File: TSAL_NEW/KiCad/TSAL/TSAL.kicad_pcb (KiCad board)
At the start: 2 copper layers, 74.8 x 41.9 mm, 33 parts, among them J1 HV INPUT, J2 HV GND, J3 Pin Storage, J4 Green_LED_Jp, J5 Conn_02x02_Counter_Clockwise, Q1 BSS84, Q2 BSS84, U1 LTV-817S, U2 LR8K4-G, U4 LM555

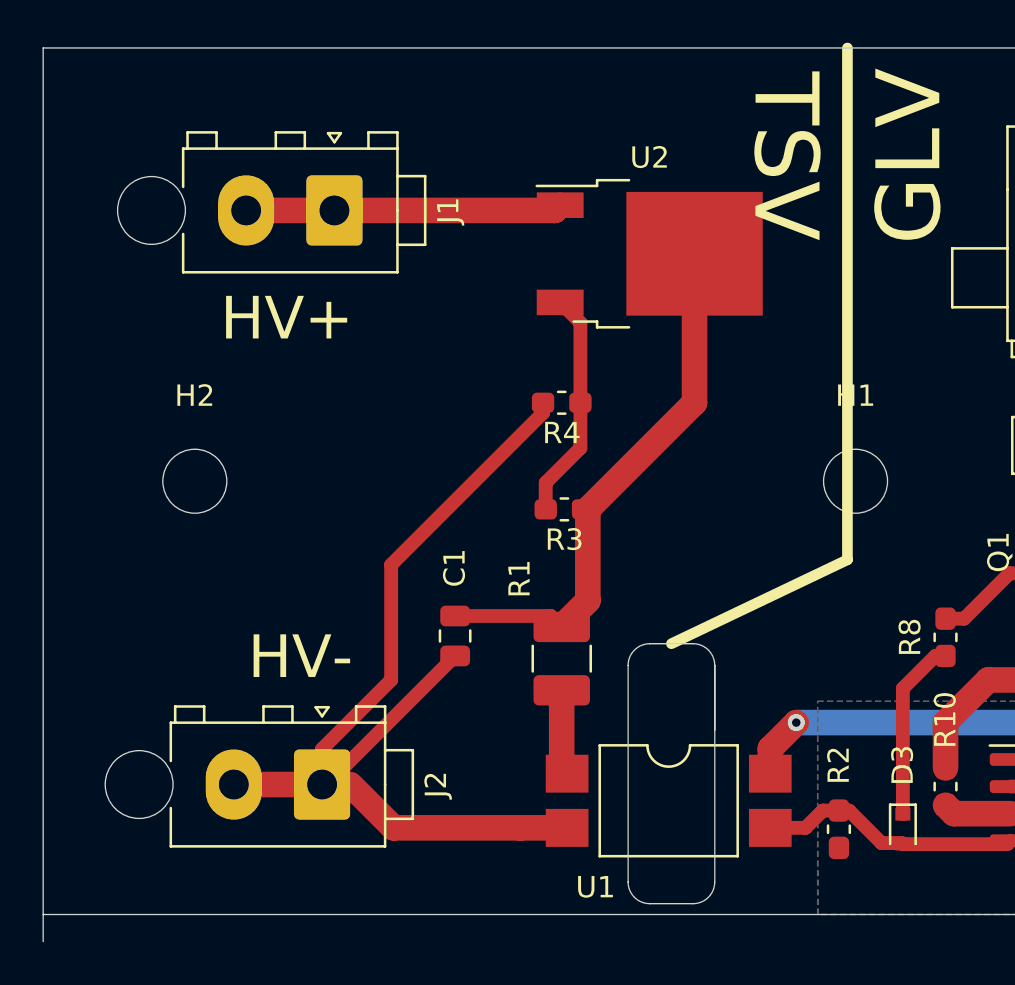
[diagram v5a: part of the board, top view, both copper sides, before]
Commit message: Added logos
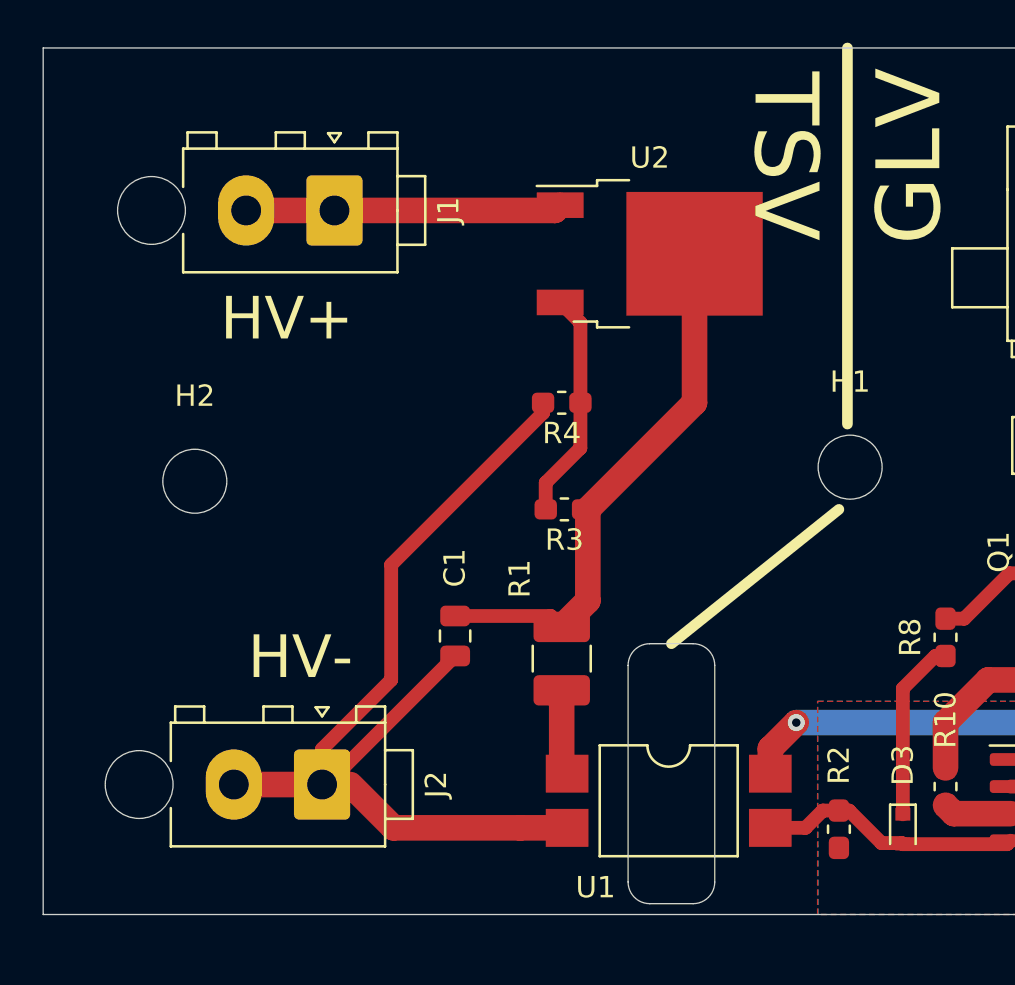
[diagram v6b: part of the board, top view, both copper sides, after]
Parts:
- added G***: LOGO, AERO-footprints:AERO_Logo_15x6mm, B.Cu at (168.0, 120.5)
- moved H1 0.71 mm to (144.5, 106.0)
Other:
- board size 74.8 x 41.9 mm -> 74.8 x 40.6 mm
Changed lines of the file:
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@@
   (general
     (thickness 1.6)
-    (drawings 27)
+    (drawings 26)
     (tracks 116)
     (zones 0)
-    (modules 33)
+    (modules 34)
     (nets 24)
   )
@@
   )
   (setup
-    (last_trace_width 0.65)
+    (last_trace_width 0.25)
     (user_trace_width 0.24)
     (user_trace_width 0.36)
@@
     (add_net GNDA)
   )
+  (module AERO-footprints:AERO_Logo_15x6mm (layer B.Cu)
+    (at 168 120.5 180)
+    (fp_text reference G*** (at 0 0) (layer B.SilkS) hide
+      (effects (font (size 1.524 1.524) (thickness 0.3)) (justify mirror))
+    )
+    (fp_text value LOGO (at 0.75 0) (layer B.SilkS) hide
+      (effects (font (size 1.524 1.524) (thickness 0.3)) (justify mirror))
+    )
+    (fp_poly (pts (xy 6.892292 2.256606) (xy 7.522038 1.627588) (xy 7.522038 -1.522592) (xy 6.209332 -2.833934)
+      (xy 5.038016 -1.661096) (xy 5.038016 -1.378625) (xy 5.912672 -1.378625) (xy 6.024987 -1.494504)
+      (xy 6.137301 -1.610384) (xy 6.374849 -1.374656) (xy 6.612397 -1.138929) (xy 6.612397 1.208337)
+      (xy 6.262534 1.556887) (xy 5.912672 1.905436) (xy 5.912672 -1.378625) (xy 5.038016 -1.378625)
+      (xy 5.038016 1.662595) (xy 5.650281 2.27411) (xy 6.262545 2.885624) (xy 6.892292 2.256606)) (layer B.SilkS) (width 0.01))
+    (fp_poly (pts (xy 4.085094 2.369879) (xy 4.583195 1.870887) (xy 4.583195 0.963505) (xy 3.972357 0.349823)
+      (xy 4.295269 0.025563) (xy 4.618182 -0.298698) (xy 4.618182 -1.659646) (xy 4.801166 -1.844931)
+      (xy 4.984149 -2.030217) (xy 4.180096 -2.83427) (xy 3.395312 -2.046694) (xy 3.567904 -1.85427)
+      (xy 3.740497 -1.661846) (xy 3.742011 -1.206428) (xy 3.743526 -0.751011) (xy 3.358678 -0.367356)
+      (xy 2.973829 0.0163) (xy 2.973829 -1.699463) (xy 3.149146 -1.872144) (xy 3.324464 -2.044825)
+      (xy 2.931053 -2.439355) (xy 2.796179 -2.57326) (xy 2.678343 -2.687693) (xy 2.586396 -2.774262)
+      (xy 2.529184 -2.824577) (xy 2.515023 -2.833884) (xy 2.484378 -2.809858) (xy 2.414426 -2.743504)
+      (xy 2.313856 -2.643412) (xy 2.191358 -2.518171) (xy 2.10951 -2.433024) (xy 1.726618 -2.032164)
+      (xy 1.912896 -1.8482) (xy 2.099173 -1.664236) (xy 2.099173 0.472657) (xy 2.903857 0.472657)
+      (xy 3.349759 0.91856) (xy 3.795662 1.364463) (xy 2.903857 2.256268) (xy 2.903857 0.472657)
+      (xy 2.099173 0.472657) (xy 2.099173 1.764775) (xy 1.898879 1.967182) (xy 1.698585 2.169588)
+      (xy 2.046914 2.519229) (xy 2.395244 2.86887) (xy 3.586993 2.86887) (xy 4.085094 2.369879)) (layer B.SilkS) (width 0.01))
+    (fp_poly (pts (xy -2.126864 2.214321) (xy -1.487961 1.574717) (xy -1.819235 1.24206) (xy -2.150508 0.909403)
+      (xy -2.632141 1.390114) (xy -3.113774 1.870826) (xy -3.113774 0.416909) (xy -2.449463 0.427118)
+      (xy -1.785151 0.437328) (xy -2.212781 0.008746) (xy -2.64041 -0.419835) (xy -3.113774 -0.419835)
+      (xy -3.113774 -1.430874) (xy -2.989067 -1.525994) (xy -2.864359 -1.621113) (xy -2.507589 -1.265558)
+      (xy -2.15082 -0.910002) (xy -1.835197 -1.225625) (xy -1.519575 -1.541248) (xy -2.169155 -2.187566)
+      (xy -2.34366 -2.360587) (xy -2.501708 -2.516125) (xy -2.636615 -2.647697) (xy -2.741696 -2.748821)
+      (xy -2.810268 -2.813012) (xy -2.835454 -2.833884) (xy -2.863865 -2.810205) (xy -2.934415 -2.7438)
+      (xy -3.039961 -2.641616) (xy -3.173361 -2.510602) (xy -3.327474 -2.357704) (xy -3.420301 -2.264972)
+      (xy -3.98843 -1.69606) (xy -3.98843 1.624396) (xy -3.377098 2.23916) (xy -2.765766 2.853925)
+      (xy -2.126864 2.214321)) (layer B.SilkS) (width 0.01))
+    (fp_poly (pts (xy -5.221339 2.265012) (xy -4.618182 1.661116) (xy -4.618182 -1.659646) (xy -4.435198 -1.844931)
+      (xy -4.252214 -2.030217) (xy -4.654241 -2.432243) (xy -5.056267 -2.83427) (xy -5.457346 -2.43205)
+      (xy -5.858424 -2.02983) (xy -5.492838 -1.659646) (xy -5.492838 -0.944628) (xy -6.262535 -0.944628)
+      (xy -6.262535 -1.659646) (xy -6.079551 -1.844931) (xy -5.896567 -2.030217) (xy -6.70062 -2.83427)
+      (xy -7.502776 -2.02983) (xy -7.319984 -1.844738) (xy -7.13719 -1.659646) (xy -7.13719 -0.034986)
+      (xy -6.262535 -0.034986) (xy -5.492838 -0.034986) (xy -5.492838 1.10401) (xy -5.875913 1.50538)
+      (xy -6.258989 1.906749) (xy -6.260762 0.935881) (xy -6.262535 -0.034986) (xy -7.13719 -0.034986)
+      (xy -7.13719 1.557578) (xy -6.480843 2.213243) (xy -5.824495 2.868909) (xy -5.221339 2.265012)) (layer B.SilkS) (width 0.01))
+    (fp_poly (pts (xy 0.892149 2.064187) (xy 0.53294 1.084573) (xy 1.076576 1.084573) (xy 1.281642 1.084154)
+      (xy 1.425832 1.082139) (xy 1.518241 1.077389) (xy 1.567965 1.068766) (xy 1.5841 1.055131)
+      (xy 1.575739 1.035346) (xy 1.565711 1.023347) (xy 1.537708 0.986527) (xy 1.472995 0.898463)
+      (xy 1.375622 0.764785) (xy 1.24964 0.591123) (xy 1.0991 0.383107) (xy 0.928052 0.146367)
+      (xy 0.740547 -0.113466) (xy 0.540636 -0.390763) (xy 0.33237 -0.679893) (xy 0.1198 -0.975227)
+      (xy -0.093025 -1.271134) (xy -0.302053 -1.561985) (xy -0.503233 -1.842148) (xy -0.692515 -2.105995)
+      (xy -0.865847 -2.347895) (xy -1.019181 -2.562217) (xy -1.148463 -2.743333) (xy -1.249645 -2.885611)
+      (xy -1.318674 -2.983422) (xy -1.351501 -3.031136) (xy -1.35222 -3.032265) (xy -1.349457 -3.013674)
+      (xy -1.325691 -2.935209) (xy -1.282989 -2.803056) (xy -1.223417 -2.623402) (xy -1.149041 -2.402431)
+      (xy -1.061928 -2.146332) (xy -0.964145 -1.861288) (xy -0.871159 -1.592142) (xy -0.764276 -1.283551)
+      (xy -0.664769 -0.995885) (xy -0.574915 -0.735757) (xy -0.496994 -0.509778) (xy -0.433282 -0.32456)
+      (xy -0.386058 -0.186716) (xy -0.357599 -0.102858) (xy -0.349862 -0.078987) (xy -0.382823 -0.075836)
+      (xy -0.473606 -0.073166) (xy -0.610059 -0.071186) (xy -0.780034 -0.070108) (xy -0.869786 -0.069973)
+      (xy -1.389709 -0.069973) (xy -0.998949 0.81343) (xy -0.875406 1.092997) (xy -0.742067 1.395195)
+      (xy -0.60729 1.701053) (xy -0.479431 1.9916) (xy -0.366846 2.247865) (xy -0.313152 2.370317)
+      (xy -0.018117 3.043801) (xy 1.251357 3.043801) (xy 0.892149 2.064187)) (layer B.SilkS) (width 0.01))
+  )
   (module MountingHole:MountingHole_3mm (layer F.Cu)
     (at 113.792 106.68)
@@
   )
   (module MountingHole:MountingHole_3mm (layer F.Cu)
-    (at 144.78 106.68)
+    (at 144.526 106.0196)
     (descr "Mounting Hole 3mm, no annular")
     (tags "mounting hole 3mm no annular")
@@
     )
   )
+  (gr_line (start 138.176 125.476) (end 138.176 115.316) (layer Edge.Cuts) (width 0.05))
+  (gr_arc (start 137.16 115.316) (end 138.176 115.316) (angle -90) (layer Edge.Cuts) (width 0.05))
   (gr_line (start 181.5 127) (end 181.5 86.36) (layer Edge.Cuts) (width 0.05))
   (gr_line (start 135.128 126.492) (end 137.16 126.492) (layer Edge.Cuts) (width 0.05))
   (gr_line (start 137.16 114.3) (end 135.128 114.3) (layer Edge.Cuts) (width 0.05))
   (gr_arc (start 135.128 115.316) (end 135.128 114.3) (angle -90) (layer Edge.Cuts) (width 0.05))
-  (gr_arc (start 137.16 115.316) (end 138.176 115.316) (angle -90) (layer Edge.Cuts) (width 0.05))
   (gr_arc (start 135.128 125.476) (end 134.112 125.476) (angle -90) (layer Edge.Cuts) (width 0.05))
   (gr_arc (start 137.16 125.476) (end 137.16 126.492) (angle -90) (layer Edge.Cuts) (width 0.05))
-  (gr_line (start 138.176 115.316) (end 138.176 125.476) (layer Edge.Cuts) (width 0.05))
   (gr_line (start 134.112 125.476) (end 134.112 115.316) (layer Edge.Cuts) (width 0.05))
-  (gr_line (start 138.176 115.316) (end 138.176 118.364) (layer Edge.Cuts) (width 0.05))
   (dimension 40.64 (width 0.12) (layer F.SilkS)
     (gr_text "40.640 mm" (at 186.58 106.68 270) (layer F.SilkS)
@@
   )
   (gr_line (start 181.5 86.36) (end 106.68 86.36) (layer Edge.Cuts) (width 0.05))
-  (gr_line (start 106.68 128.27) (end 106.68 86.36) (layer Edge.Cuts) (width 0.05))
+  (gr_line (start 106.68 127) (end 106.68 86.36) (layer Edge.Cuts) (width 0.05))
   (gr_line (start 181.5 127) (end 106.68 127) (layer Edge.Cuts) (width 0.05))
   (dimension 11 (width 0.12) (layer F.SilkS)
@@
     (effects (font (size 3 3) (thickness 0.2)))
   )
-  (gr_line (start 144.399 110.363) (end 144.399 86.36) (layer F.SilkS) (width 0.5))
+  (gr_line (start 144.399 104) (end 144.399 86.36) (layer F.SilkS) (width 0.5))
   (gr_text TSV (at 141.478 91.44 270) (layer F.SilkS)
     (effects (font (size 3 3) (thickness 0.3)))
   )
-  (gr_line (start 136.144 114.3) (end 144.399 110.363) (layer F.SilkS) (width 0.5))
+  (gr_line (start 136.144 114.3) (end 144 108) (layer F.SilkS) (width 0.5))
   (gr_text GLV (at 147.32 91.44 270) (layer B.SilkS)
     (effects (font (size 3 3) (thickness 0.2)) (justify mirror))
@@
     (effects (font (size 3 3) (thickness 0.3)) (justify mirror))
   )
-  (gr_line (start 144.399 110.363) (end 144.399 86.36) (layer B.SilkS) (width 0.5))
-  (gr_line (start 136.271 114.3) (end 144.399 110.363) (layer B.SilkS) (width 0.5))
+  (gr_line (start 144.399 104) (end 144.399 86.36) (layer B.SilkS) (width 0.5))
+  (gr_line (start 136.271 114.3) (end 144 108) (layer B.SilkS) (width 0.5))
   (via (at 154.6 119.8) (size 0.8) (drill 0.4) (layers F.Cu B.Cu) (net 1))
   (via (at 174 124) (size 0.8) (drill 0.4) (layers F.Cu B.Cu) (net 1))

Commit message: Layout Rev2
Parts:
- removed G***: LOGO, AERO-footprints:AERO_Logo_15x6mm
- added R12: 10k, Resistor_SMD:R_0603_1608Metric_Pad1.05x0.95mm_HandSolder, F.Cu at (162.2, 103.6)
- added R13: R, Resistor_SMD:R_0603_1608Metric_Pad1.05x0.95mm_HandSolder, F.Cu at (164.2, 109.5)
- added R14: R, Resistor_SMD:R_0603_1608Metric_Pad1.05x0.95mm_HandSolder, F.Cu at (164.2, 107.2)
- added TH1: Thermistor, Resistor_SMD:R_0603_1608Metric_Pad1.05x0.95mm_HandSolder, F.Cu at (165.1, 103.6)
- J3: value Pin Storage -> Conn_01x03; footprint Connector_PinHeader_2.54mm:PinHeader_1x02_P2.54mm_Vertical -> Connector_JST:JST_PH_B3B-PH-K_1x03_P2.00mm_Vertical
- J4: value Green_LED_Jp -> Conn_01x04; footprint Connector_PinHeader_2.54mm:PinHeader_1x02_P2.54mm_Vertical -> Connector_JST:JST_PH_B4B-PH-K_1x04_P2.00mm_Vertical
- J5: value Conn_02x02_Counter_Clockwise -> Conn_01x02; footprint Connector_TE-Connectivity:TE_MATE-N-LOK_1-770874-x_2x02_P4.14mm_Vertical -> Connector_JST:JST_PH_B2B-PH-K_1x02_P2.00mm_Vertical
- moved J4 16.0 mm to (163.7, 91.0), turned to 180 degrees
- moved J3 9.24 mm to (156.7, 101.0), turned to 90 degrees
- moved J5 7.51 mm to (163.4, 99.0), turned to 90 degrees
- moved R8 6.57 mm to (154.9, 111.1)
- moved Q1 3.59 mm to (156.1, 107.0)
- moved R9 3.11 mm to (159.1, 107.1)
- moved Q2 2.98 mm to (158.4, 113.3)
- moved R11 2.48 mm to (164.6, 115.1)
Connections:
- J3 pad 1: Net-(J3-Pad1) -> (no net)
- J3 pad 2: Net-(J3-Pad2) -> /LED_GREEN_OUT
- J4 pad 1: /LED_GREEN_OUT -> GND
- J4 pad 2: /LED_GREEN+ -> /GLV+
- J5 pad 1: /GLV+ -> /THM
- U4 pad 5: Net-(U4-Pad5) -> (no net)
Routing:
- net +12V: track 76.3 -> 85.1 mm, vias 4 -> 3
- net /THM: track 0.00 -> 6.43 mm
- net Net-(R13-Pad2): track 0.00 -> 5.79 mm
- net Net-(D3-Pad1): track 8.53 -> 13.9 mm
- net /LED_GREEN_OUT: track 9.04 -> 14.0 mm
- net Net-(Q1-Pad1): track 4.93 -> 2.26 mm
- net /GLV+: track 11.8 -> 9.59 mm
- net /LED_GREEN+: track 8.44 -> 6.46 mm
- net /RED_FET: track 9.00 -> 10.9 mm
- net /LED_RED+: track 28.0 -> 29.8 mm
- net GND: vias 9 -> 8
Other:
- outline, holes or cut-outs redrawn
- board text added: "12"
- board text added: "G"
- board text added: "GND"
- board text added: "Green Jumper"
- board text added: "R"
- board text added: "Temp"

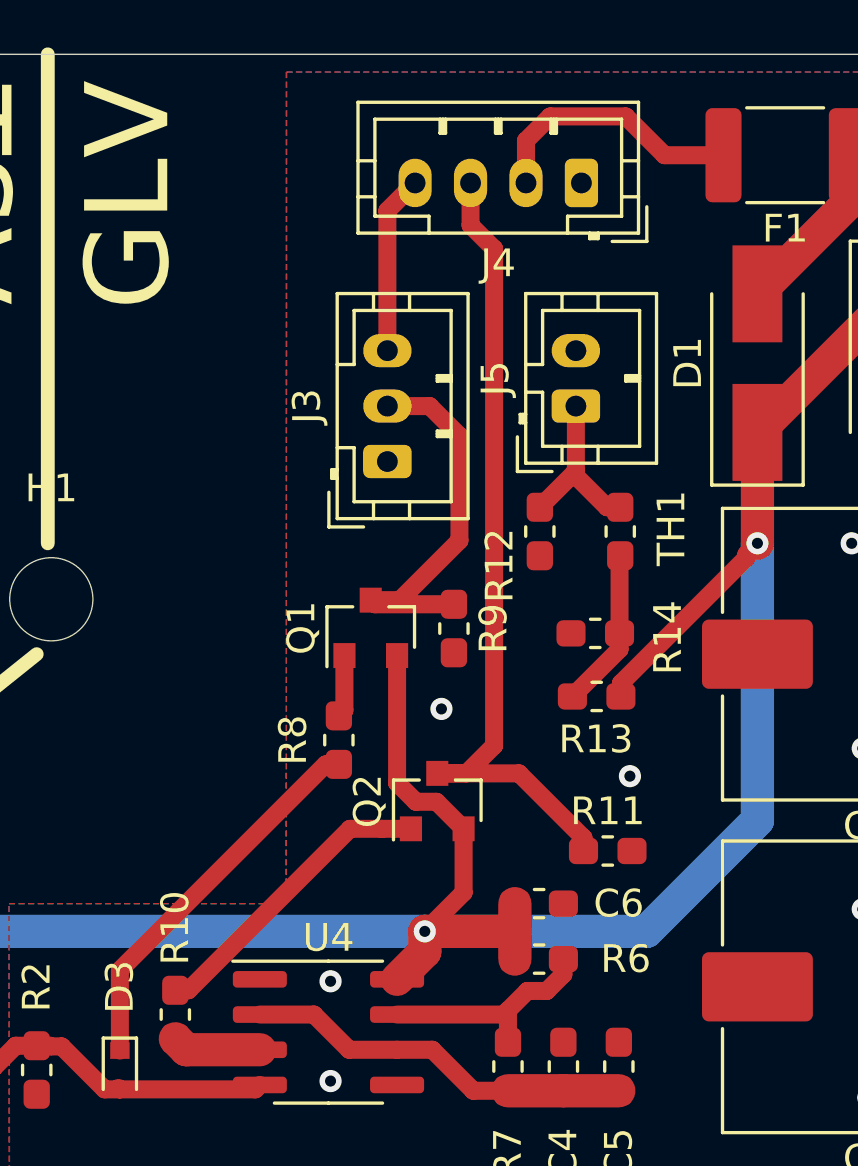
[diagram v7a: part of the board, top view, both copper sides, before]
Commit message: added LED resistors on output
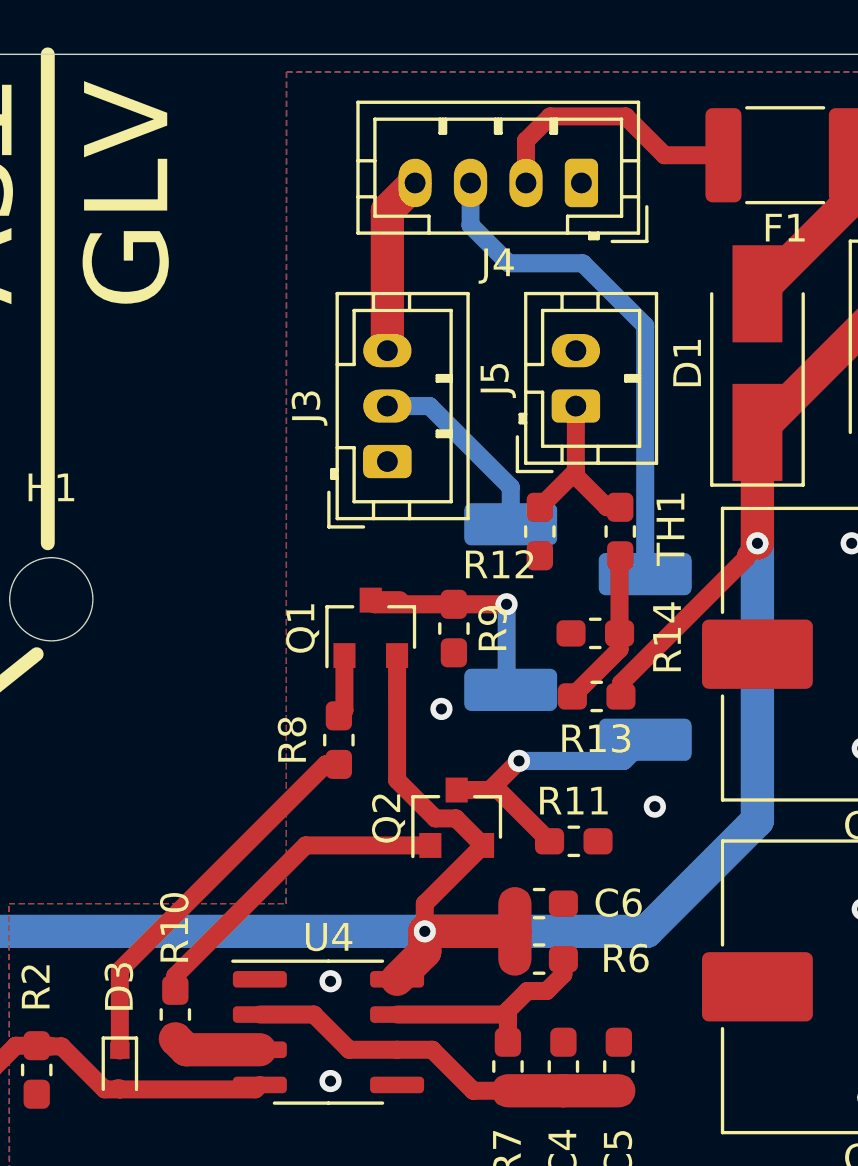
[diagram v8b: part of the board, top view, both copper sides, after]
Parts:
- added R15: 100, Resistor_SMD:R_2512_6332Metric_Pad1.52x3.35mm_HandSolder, B.Cu at (161.1, 106.3)
- added R16: 100, Resistor_SMD:R_2512_6332Metric_Pad1.52x3.35mm_HandSolder, B.Cu at (165.9, 108.1)
- moved R11 1.27 mm to (163.4, 114.8)
- moved Q2 0.92 mm to (159.2, 113.9)
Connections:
- Q1 pad 3: /LED_GREEN_OUT -> Net-(Q1-Pad3)
- Q2 pad 3: /LED_RED+ -> Net-(Q2-Pad3)
- R11 pad 1: /LED_RED+ -> Net-(Q2-Pad3)
- R9 pad 1: /LED_GREEN_OUT -> Net-(Q1-Pad3)
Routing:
- net Net-(Q2-Pad3): track 0.00 -> 11.7 mm, vias 0 -> 1
- net /LED_RED+: track 29.8 -> 18.3 mm
- net Net-(Q1-Pad3): track 0.00 -> 9.16 mm, vias 0 -> 1
- net /LED_GREEN_OUT: track 14.0 -> 7.00 mm
- net /RED_FET: track 10.9 -> 11.7 mm
- net +12V: track 85.1 -> 85.7 mm
